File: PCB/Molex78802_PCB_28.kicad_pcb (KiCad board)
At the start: 2 copper layers, 16.6 x 38 mm, 1 part

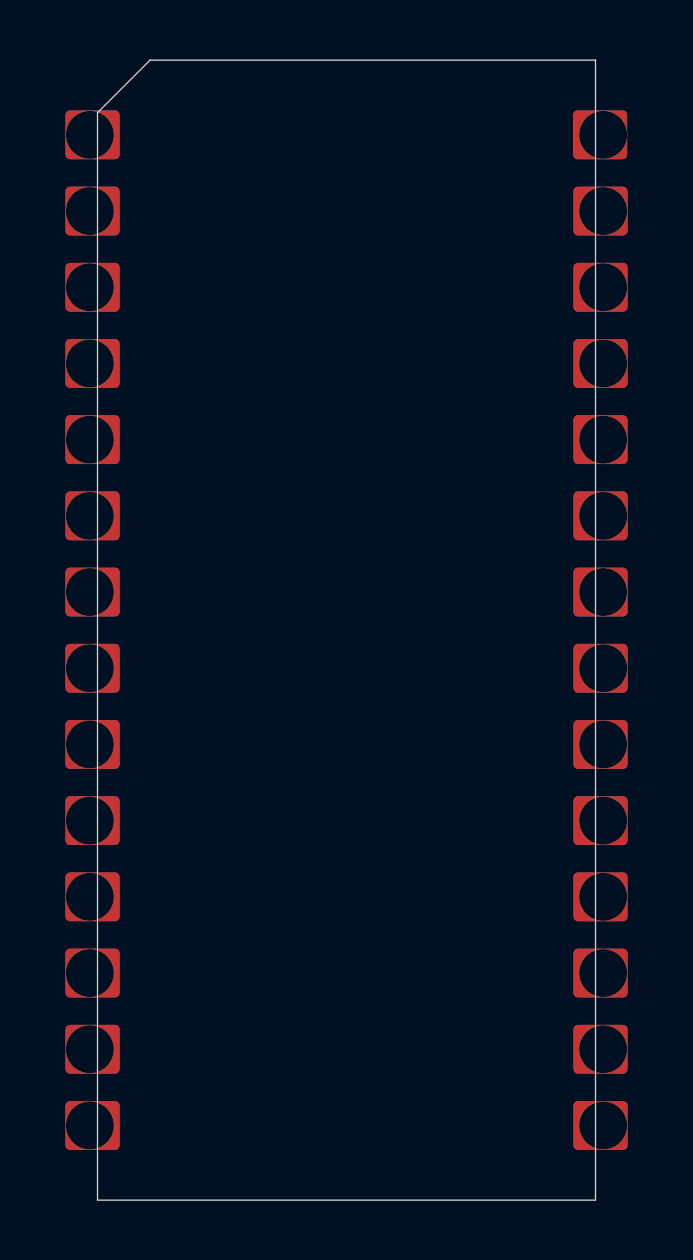
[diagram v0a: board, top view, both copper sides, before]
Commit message: kicad v6, better castellated pads, add slotted version
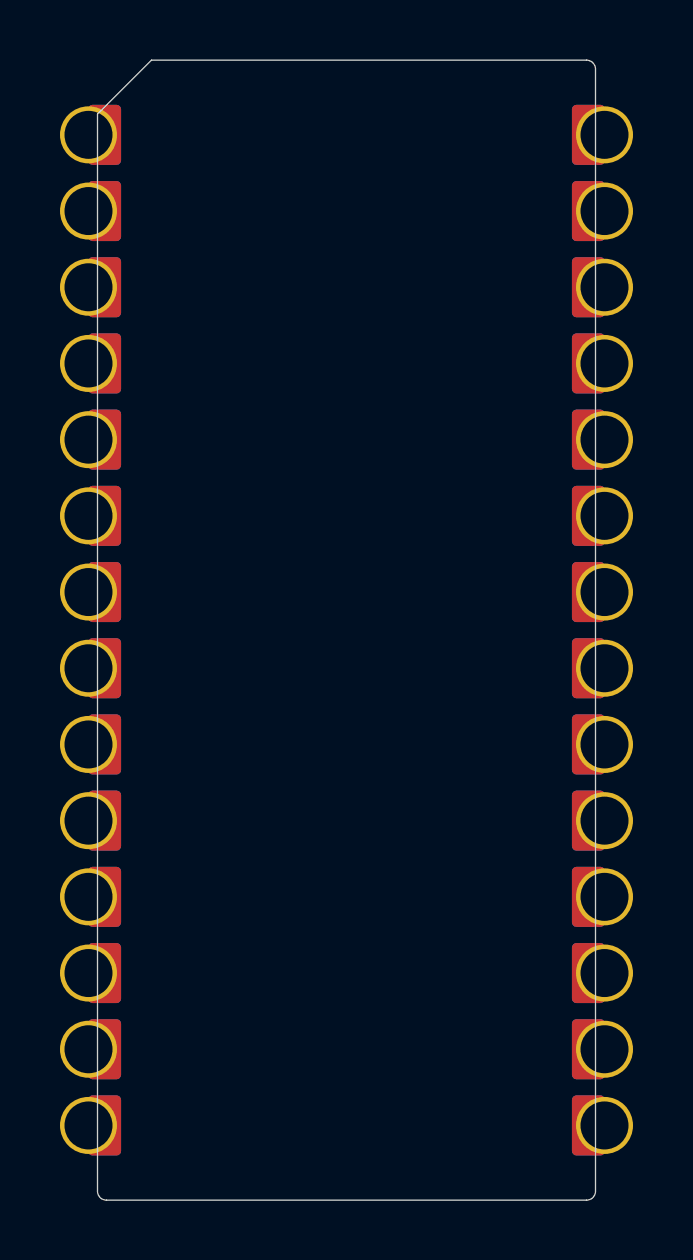
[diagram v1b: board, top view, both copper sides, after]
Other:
- outline, holes or cut-outs redrawn
- net class Default removed
